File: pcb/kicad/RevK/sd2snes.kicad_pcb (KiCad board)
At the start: 2 copper layers, 101.5 x 83 mm, 148 parts, among them J101 SNESCART_EXT, J411 Hirose DM1AA, J421 USB Mini-B SMT, P113 CONN_1, P401 CONN_7X2, P402 CONN_2, P403 CONN_2, P404 CONN_3X2, Q101 2N2222A, Q301 IRLML6402PbF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

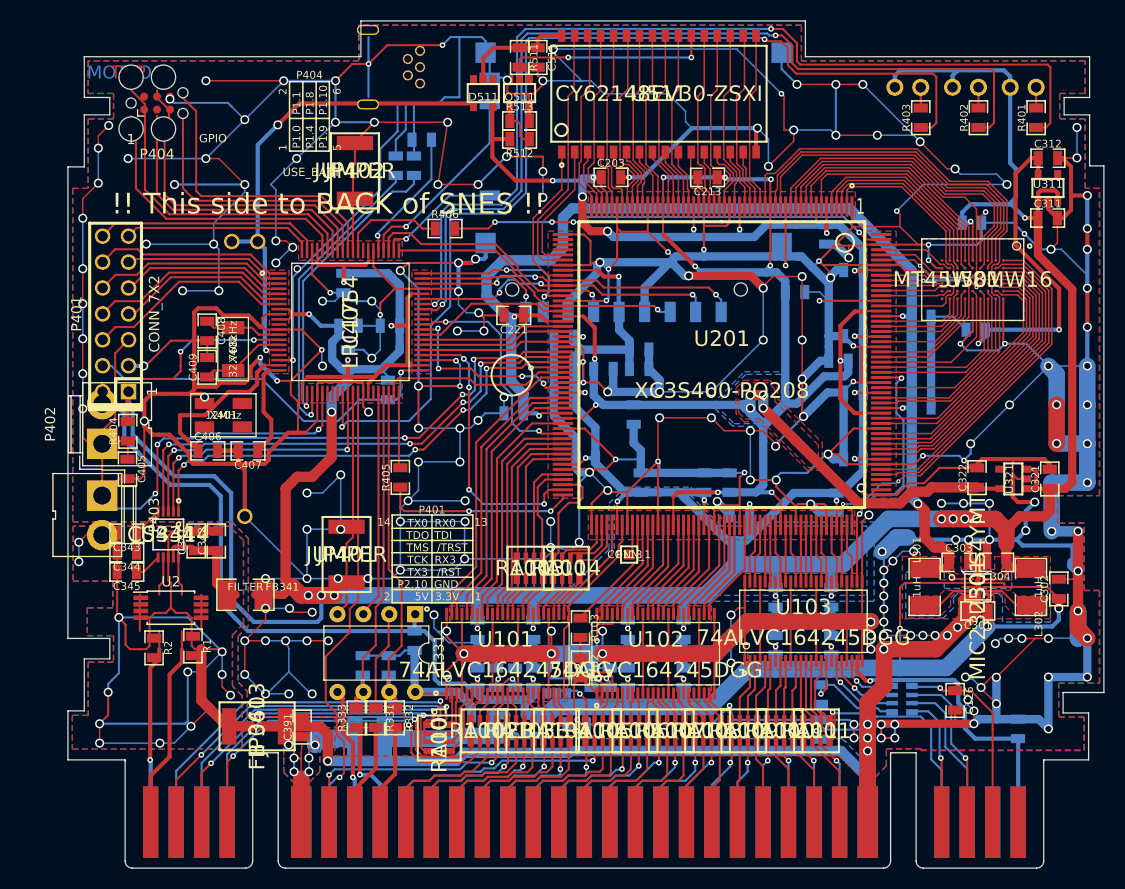
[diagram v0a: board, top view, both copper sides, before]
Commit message: Update positions and layouts to make more sense
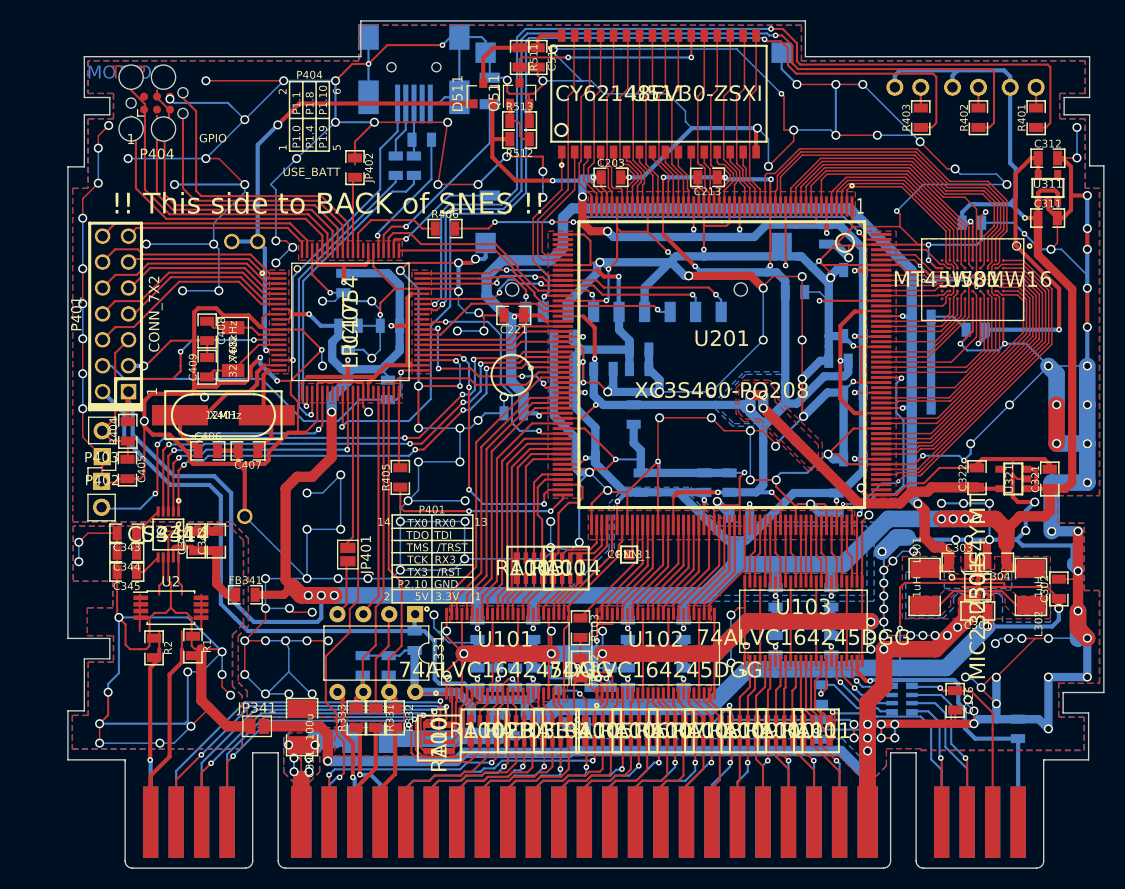
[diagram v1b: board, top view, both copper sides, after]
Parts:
- C391: footprint mypackages:SM0805_FIXEDMASK -> mypackages:SM1210L
- D511, Q101, Q511: footprint mypackages:SOT23-5_LARGEPADS -> Package_TO_SOT_SMD:SOT-23
- FB341: footprint mypackages:SM1210L -> mypackages:SM0805_FIXEDMASK
- J421: footprint mypackages:USB-MINIB-THT -> mypackages:USB_MINIB_SMT
- JP341, JP401: footprint mypackages:SMD_DO1608 -> Jumper:SolderJumper-2_P1.3mm_Open_Pad1.0x1.5mm
- JP402: footprint mypackages:SMD_DO1608 -> mypackages:SM0805_FIXEDMASK
- L391: footprint mypackages:L_4.2X4.2 -> mypackages:SM1210L
- P402, P403: footprint Connector:JWT_A3963_1x02_P3.96mm_Vertical -> Connector_PinHeader_2.54mm:PinHeader_1x02_P2.54mm_Vertical
- Q301: footprint Package_TO_SOT_SMD:SOT-23W_Handsoldering -> Package_TO_SOT_SMD:SOT-23
- X401: footprint mypackages:XTAL_SMD_05032 -> mypackages:HC49US
- moved P403 1.40 mm to (97.7, 100.2), turned to 0 degrees
- moved P402 1.27 mm to (97.8, 97.8), turned to 180 degrees
- moved JP402 0.32 mm to (122.6, 69.5), turned to 270 degrees
- moved JP401 0.13 mm to (121.9, 107.4), turned to 270 degrees
- turned D511 to 90 degrees
- turned FB341 to 0 degrees
- turned JP341 to 0 degrees
- turned L391 to 180 degrees
- turned Q101 to 270 degrees
- turned Q301 to 270 degrees
- turned Q511 to 90 degrees
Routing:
- net GNDA: track 0.00 -> 119.1 mm, vias 0 -> 13
- net AGND: track 119.1 -> 0.00 mm, vias 13 -> 0
- net Net-(P403-Pad2): track 0.00 -> 30.8 mm, vias 0 -> 3
- net N-00000314: track 30.8 -> 0.00 mm, vias 3 -> 0
- net Net-(L391-Pad1): track 40.8 -> 12.7 mm, vias 6 -> 0
- net +5VL: track 12.7 -> 40.8 mm, vias 0 -> 6
- net Net-(C123-Pad1): track 0.00 -> 7.88 mm, vias 0 -> 2
- net N-00000148: track 7.88 -> 0.00 mm, vias 2 -> 0
- net Net-(Q101-Pad2): track 0.00 -> 7.49 mm, vias 0 -> 1
- net N-0000036: track 7.49 -> 0.00 mm, vias 1 -> 0
- net Net-(Q511-Pad2): track 0.00 -> 5.05 mm
- net N-00000345: track 5.05 -> 0.00 mm

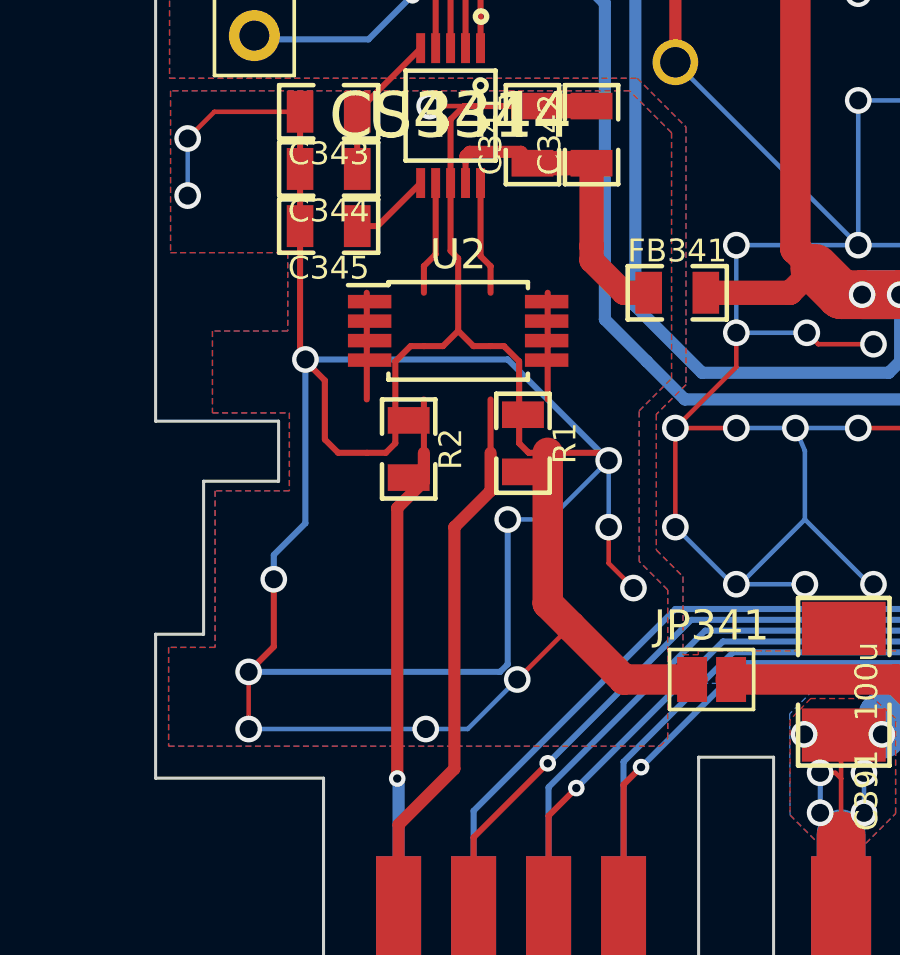
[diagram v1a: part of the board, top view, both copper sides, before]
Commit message: Update paths, fix OpAmp stuff
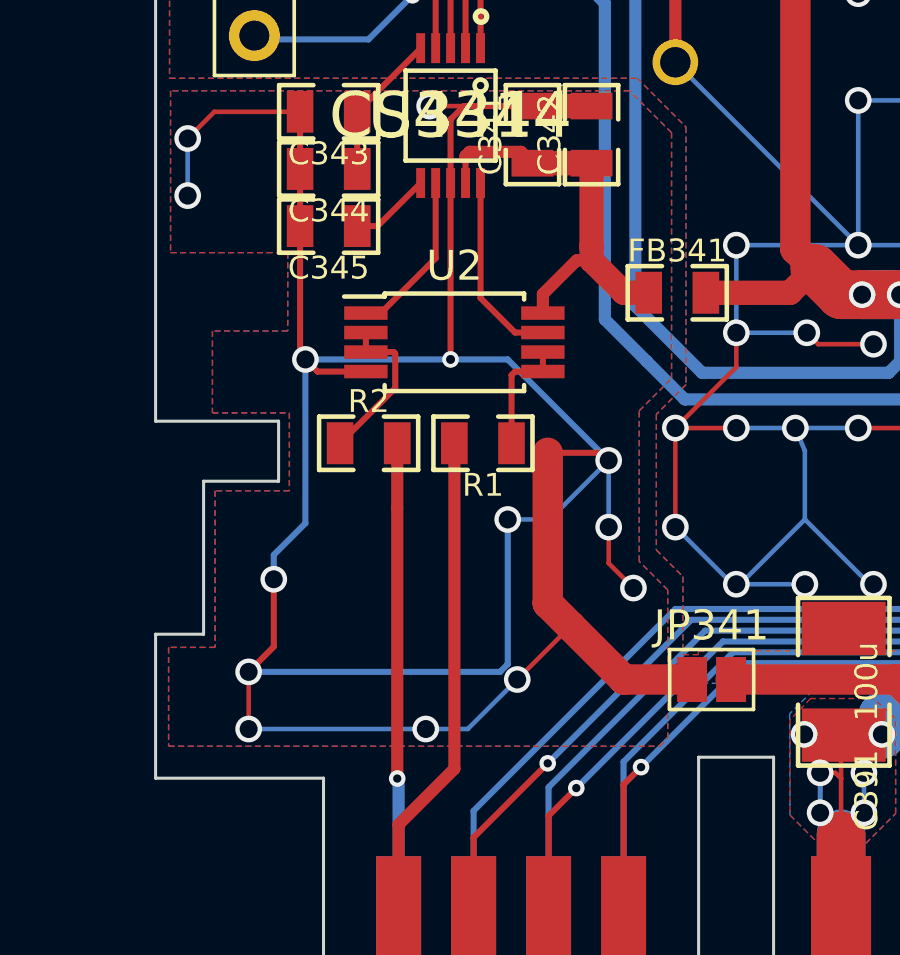
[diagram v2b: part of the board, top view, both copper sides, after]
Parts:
- moved R2 1.35 mm to (101.5, 116.3), turned to 0 degrees
- moved R1 1.33 mm to (105.3, 116.3), turned to 180 degrees
- moved U2 0.40 mm to (104.4, 113.0)
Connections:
- U103 pad 23: Net-(U103-Pad23) -> /SNES Slot/SNES_EXT_SYS_CLK
- U2 pad 2: Net-(R1-Pad1) -> Net-(R2-Pad1)
- U2 pad 3: Net-(R1-Pad1) -> Net-(R2-Pad1)
- U2 pad 5: Net-(R2-Pad1) -> Net-(R1-Pad1)
- U2 pad 6: Net-(R2-Pad1) -> Net-(R1-Pad1)
- U341 pad 10: Net-(U2-Pad1) -> Net-(U2-Pad7)
- U341 pad 7: Net-(U2-Pad7) -> Net-(U2-Pad1)
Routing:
- net GNDA: track 119.1 -> 105.0 mm, vias 13 -> 14
- net Net-(R2-Pad1): track 0.00 -> 5.66 mm
- net N-00000294: track 3.56 -> 0.00 mm
- net +3.3VDAC: track 10.9 -> 13.6 mm
- net Net-(U2-Pad7): track 3.82 -> 6.39 mm
- net AUDIO_R: track 20.0 -> 18.0 mm
- net AUDIO_L: track 19.1 -> 17.3 mm
- net Net-(U2-Pad1): track 3.80 -> 5.59 mm

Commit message: Refill zones
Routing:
- net GNDA: track 105.0 -> 106.7 mm, vias 14 -> 15
- added copper zone on B.Cu, net GNDA
- added copper zone on F.Cu, net GNDA
- removed copper zone on B.Cu, net AGND
- removed copper zone on F.Cu, net AGND

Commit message: Fix connector
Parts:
- JP402: value JUMPER -> (none)
- P113: value CONN_1 -> (none)
- P404: footprint Connector:Tag-Connect_TC2030-IDC-FP_2x03_P1.27mm_Vertical -> Connector_PinHeader_2.54mm:PinHeader_2x03_P2.54mm_Vertical
- U101, U102, U103: value 74ALVC164245DGG -> (none)
- U301: value MIC23250-S4YMT -> (none)
- U341: value CS4344 -> (none)
- U501: value MT45W8MW16 -> MT45W8
- U511: value CY62148EV30-ZSXI -> (none)
- moved P404 2.89 mm to (100.6, 64.5), turned to 90 degrees
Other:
- board text added: "Rev.K / 2019-01-01"
- board text removed: "Assembled in Ukraine"
- board text removed: "Rev.K / 2018-12-24"

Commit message: Add gnd to pin 28 of U401
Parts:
- JP402: value (none) -> JUMPER
- P113: value (none) -> CONN_1
- U101, U102, U103: value (none) -> 74ALVC164245DGG
- U301: value (none) -> MIC23250-S4YMT
- U341: value (none) -> CS4344
- U501: value MT45W8 -> MT45W8MW16
- U511: value (none) -> CY62148EV30-ZSXI
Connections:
- U401 pad 28: Net-(U401-Pad28) -> GND
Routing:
- net GND: track 1917.6 -> 1918.6 mm

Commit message: Minor fixes in layout
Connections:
- D511 pad 1: +3.3V -> +BATT
- D511 pad 2: +BATT -> +3.3V
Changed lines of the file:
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@@
       (net 10 /Memory/SRAM_Vcc))
     (pad 2 smd rect (at -1 0.95 90) (size 0.9 0.8) (layers Component F.Paste F.Mask)
+      (net 4 +3.3V))
+    (pad 1 smd rect (at -1 -0.95 90) (size 0.9 0.8) (layers Component F.Paste F.Mask)
       (net 8 +BATT))
-    (pad 1 smd rect (at -1 -0.95 90) (size 0.9 0.8) (layers Component F.Paste F.Mask)
-      (net 4 +3.3V))
     (model ${KISYS3DMOD}/Package_TO_SOT_SMD.3dshapes/SOT-23.wrl
       (at (xyz 0 0 0))

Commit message: Update Layout for Resistor Arrays
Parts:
- RA101, RA102, RA103, RA104, RA105, RA106, RA107, RA108, RA109, RA110, RA111, RA112, RA113, RA114: footprint mypackages:R_PACK_1206 -> mypackages:R_PACK_1206_2
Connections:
- Q101 pad 1: GND -> Net-(C123-Pad1)
- Q101 pad 3: Net-(C123-Pad1) -> GND
